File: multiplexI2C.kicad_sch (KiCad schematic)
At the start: 25 parts, among them J17 Conn_01x04_Pin, J18 PinSocket_1x20_P2.54mm_Vertic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, J19 PinSocket_1x20_P2.54mm_Vertic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, J20 Screw_Terminal_01x02, U1 PCA9548ADW

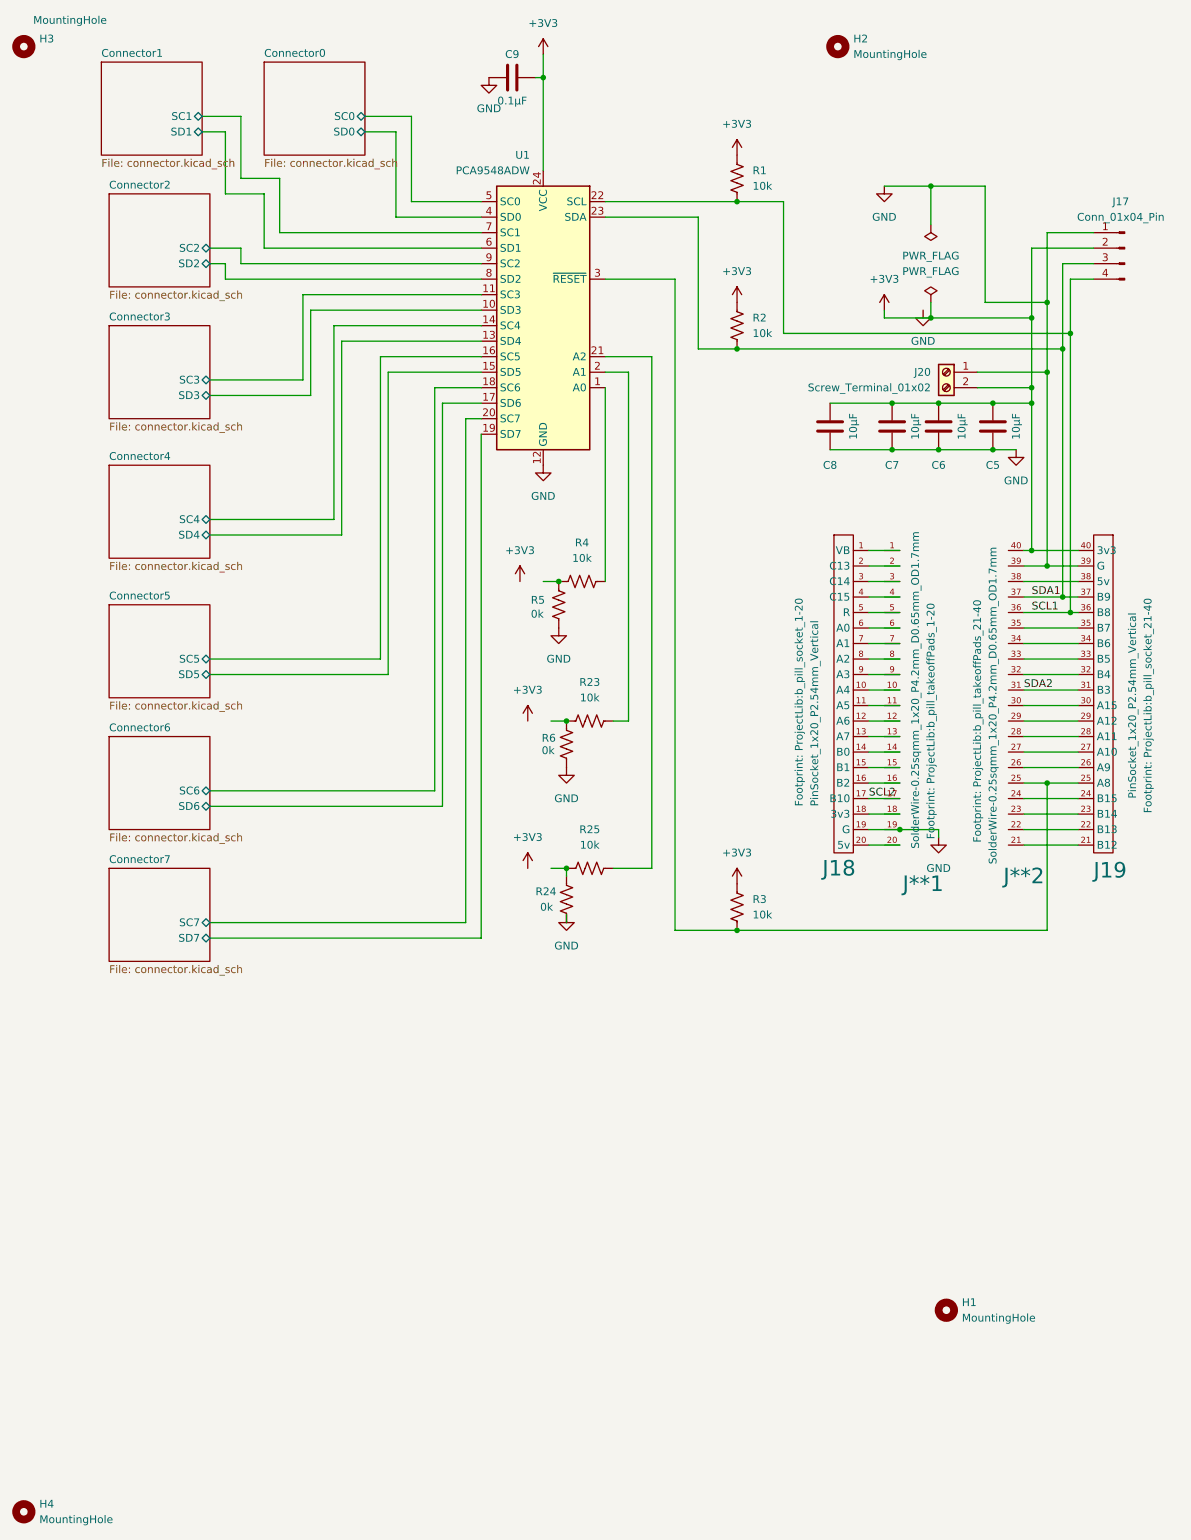
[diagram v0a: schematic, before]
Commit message: ERC and DRC warnings but not erros. Needs some layout adjustments.
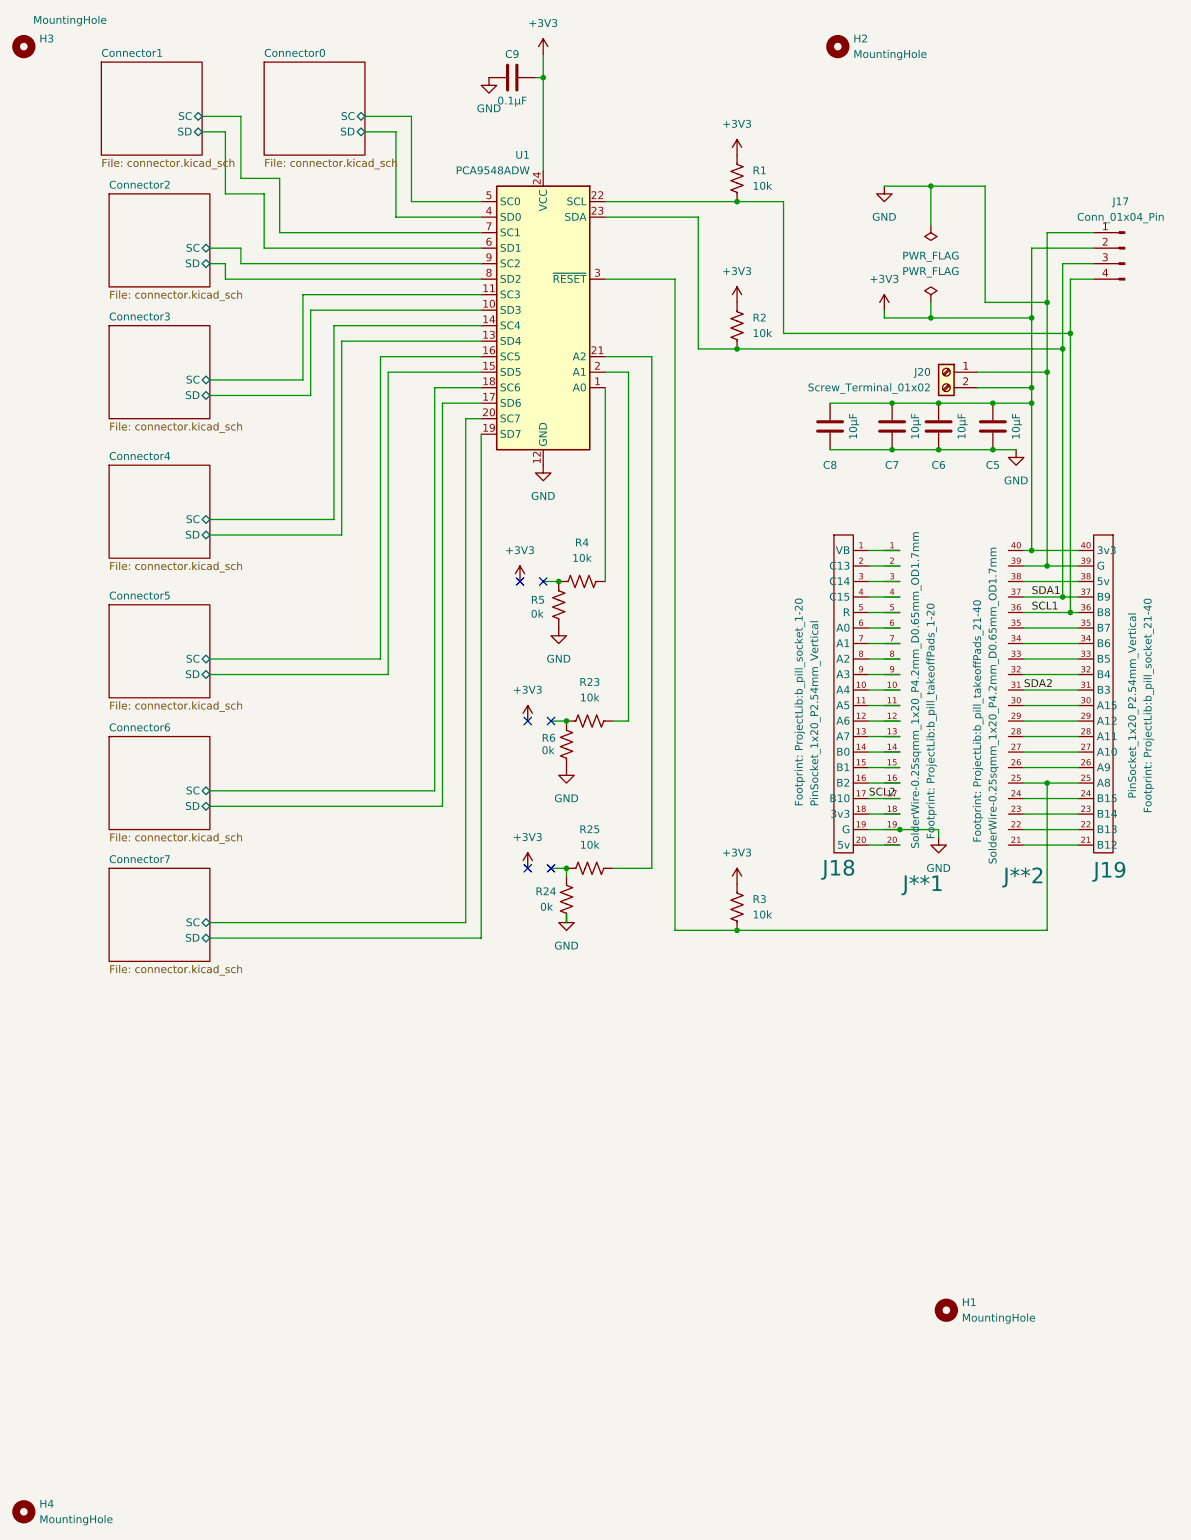
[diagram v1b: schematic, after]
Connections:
- net Connector0/SC0 renamed Connector0/SC
- net Connector0/SD0 renamed Connector0/SD
- net Connector1/SC1 renamed Connector1/SC
- net Connector1/SD1 renamed Connector1/SD
- net Connector2/SC2 renamed Connector2/SC
- net Connector2/SD2 renamed Connector2/SD
- net Connector3/SC3 renamed Connector3/SC
- net Connector3/SD3 renamed Connector3/SD
- net Connector4/SC4 renamed Connector4/SC
- net Connector4/SD4 renamed Connector4/SD
- net Connector5/SC5 renamed Connector5/SC
- net Connector5/SD5 renamed Connector5/SD
- net Connector6/SC6 renamed Connector6/SC
- net Connector6/SD6 renamed Connector6/SD
- net Connector7/SC7 renamed Connector7/SC
- net Connector7/SD7 renamed Connector7/SD
- no-connect marks 0 -> 6
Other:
- sheet Connector0 ports: added SC, SD; removed SC0, SD0
- sheet Connector1 ports: added SC, SD; removed SC1, SD1
- sheet Connector2 ports: added SC, SD; removed SC2, SD2
- sheet Connector3 ports: added SC, SD; removed SC3, SD3
- sheet Connector4 ports: added SC, SD; removed SC4, SD4
- sheet Connector5 ports: added SC, SD; removed SC5, SD5
- sheet Connector6 ports: added SC, SD; removed SC6, SD6
- sheet Connector7 ports: added SC, SD; removed SC7, SD7
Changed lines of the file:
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@@
 		(color 0 0 0 0)
 	)
+	(no_connect
+		(at 105.41 130.81)
+	)
+	(no_connect
+		(at 104.14 107.95)
+	)
+	(no_connect
+		(at 105.41 154.94)
+	)
+	(no_connect
+		(at 101.6 154.94)
+	)
+	(no_connect
+		(at 101.6 130.81)
+	)
+	(no_connect
+		(at 100.33 107.95)
+	)
 	(wire
 		(pts
@@
 	)
 	(symbol
-		(lib_name "GND_1")
-		(lib_id "power:GND")
-		(at 166.37 63.5 0)
-		(unit 1)
-		(exclude_from_sim no)
-		(in_bom yes)
-		(on_board yes)
-		(dnp no)
-		(fields_autoplaced yes)
-		(property "Reference" "#PWR028"
-			(at 166.37 69.85 0)
-			(effects
-				(font
-					(size 1.27 1.27)
-				)
-				(hide yes)
-			)
-		)
-		(property "Value" "GND"
-			(at 166.37 68.58 0)
-			(effects
-				(font
-					(size 1.27 1.27)
-				)
-			)
-		)
-		(property "Footprint" ""
-			(at 166.37 63.5 0)
-			(effects
-				(font
-					(size 1.27 1.27)
-				)
-				(hide yes)
-			)
-		)
-		(property "Datasheet" ""
-			(at 166.37 63.5 0)
-			(effects
-				(font
-					(size 1.27 1.27)
-				)
-				(hide yes)
-			)
-		)
-		(property "Description" "Power symbol creates a global label with name \"GND\" , ground"
-			(at 166.37 63.5 0)
-			(effects
-				(font
-					(size 1.27 1.27)
-				)
-				(hide yes)
-			)
-		)
-		(pin "1"
-		)
-		(instances
-			(project ""
-				(path "/0c2d0c14-8850-4a30-bb78-b2f40cb442ba"
-					(reference "#PWR028")
-					(unit 1)
-				)
-			)
-		)
-	)
-	(symbol
 		(lib_id "power:GND")
 		(at 107.95 162.56 0)
@@
 			)
 		)
-		(pin "SC2" bidirectional
+		(pin "SC" bidirectional
 			(at 49.53 53.34 0)
 			(effects
@@
 			)
 		)
-		(pin "SD2" bidirectional
+		(pin "SD" bidirectional
 			(at 49.53 55.88 0)
 			(effects
@@
 			)
 		)
-		(pin "SC4" bidirectional
+		(pin "SC" bidirectional
 			(at 49.53 97.79 0)
 			(effects
@@
 			)
 		)
-		(pin "SD4" bidirectional
+		(pin "SD" bidirectional
 			(at 49.53 100.33 0)
 			(effects
@@
 			)
 		)
-		(pin "SC7" bidirectional
+		(pin "SC" bidirectional
 			(at 49.53 163.83 0)
 			(effects
@@
 			)
 		)
-		(pin "SD7" bidirectional
+		(pin "SD" bidirectional
 			(at 49.53 166.37 0)
 			(effects
@@
 			)
 		)
-		(pin "SC3" bidirectional
+		(pin "SC" bidirectional
 			(at 49.53 74.93 0)
 			(effects
@@
 			)
 		)
-		(pin "SD3" bidirectional
+		(pin "SD" bidirectional
 			(at 49.53 77.47 0)
 			(effects
@@
 			)
 		)
-		(pin "SC1" bidirectional
+		(pin "SC" bidirectional
 			(at 48.26 31.75 0)
 			(effects
@@
 			)
 		)
-		(pin "SD1" bidirectional
+		(pin "SD" bidirectional
 			(at 48.26 34.29 0)
 			(effects
@@
 			)
 		)
-		(pin "SC6" bidirectional
+		(pin "SC" bidirectional
 			(at 49.53 142.24 0)
 			(effects
@@
 			)
 		)
-		(pin "SD6" bidirectional
+		(pin "SD" bidirectional
 			(at 49.53 144.78 0)
 			(effects
@@
 		(at 58.42 22.86)
 		(size 16.51 15.24)
-		(fields_autoplaced yes)
 		(stroke
 			(width 0.1524)
@@
 			)
 		)
-		(pin "SC0" bidirectional
+		(pin "SC" bidirectional
 			(at 74.93 31.75 0)
 			(effects
@@
 			)
 		)
-		(pin "SD0" bidirectional
+		(pin "SD" bidirectional
 			(at 74.93 34.29 0)
 			(effects
@@
 			)
 		)
-		(pin "SC5" bidirectional
+		(pin "SC" bidirectional
 			(at 49.53 120.65 0)
 			(effects
@@
 			)
 		)
-		(pin "SD5" bidirectional
+		(pin "SD" bidirectional
 			(at 49.53 123.19 0)
 			(effects

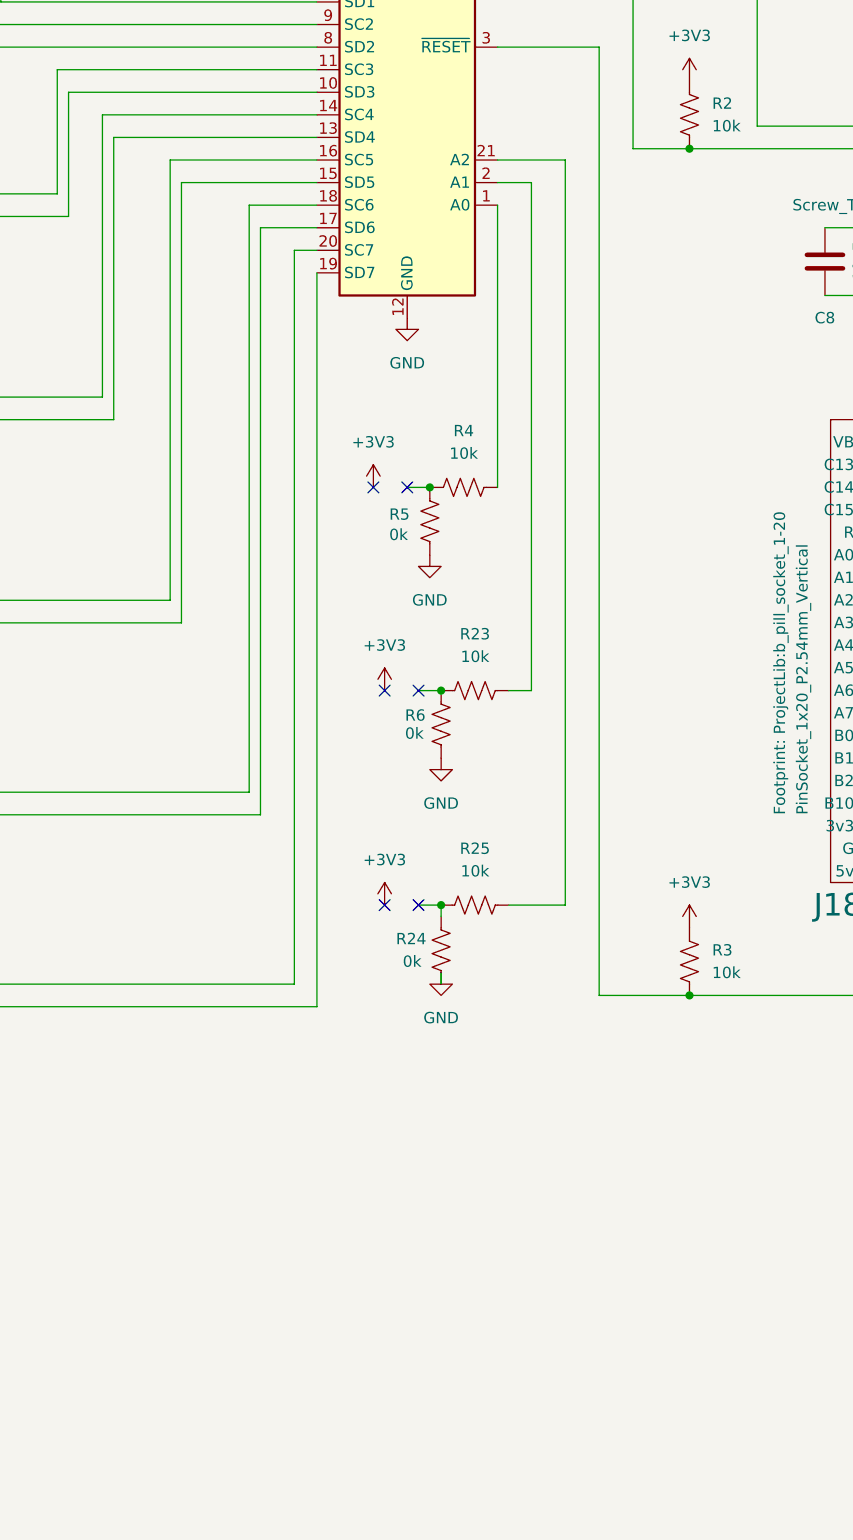
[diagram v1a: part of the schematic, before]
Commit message: no ELC or DRC errors. Still cleaning up warnings. Switched to SW_DIP for PCA9548 address.
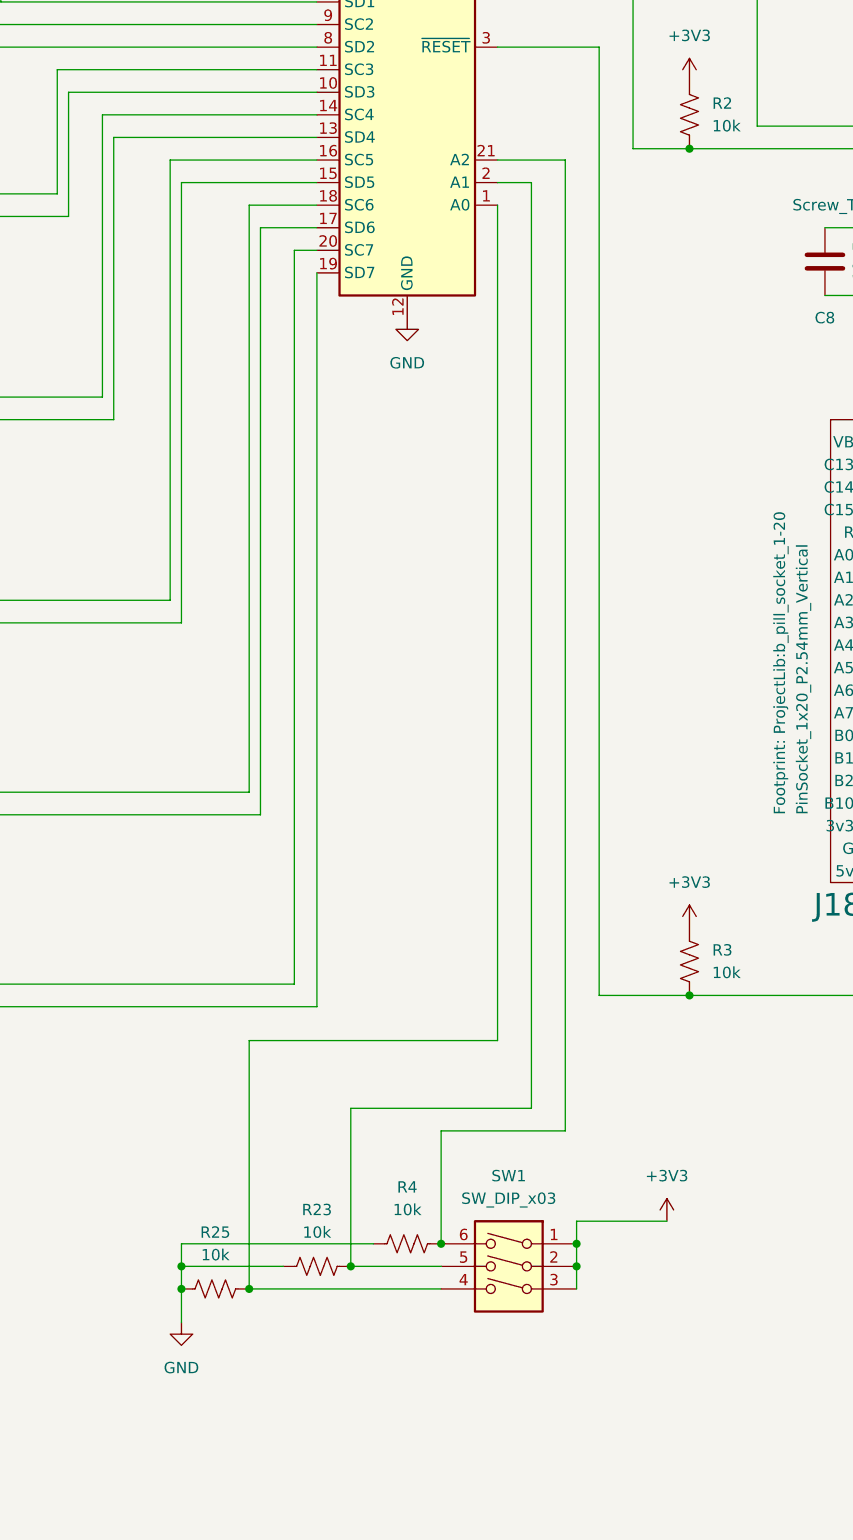
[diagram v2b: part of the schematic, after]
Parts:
- removed R24, R5, R6: 0k, ProjectLib:R_0603_1608Metric, symbol ProjectLib:R_US
- added SW1: SW_DIP_x03, Button_Switch_SMD:SW_DIP_SPSTx03_Slide_KingTek_DSHP03TS_W7.62mm_P1.27mm, symbol Switch:SW_DIP_x03
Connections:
- net +3V3: now also SW1.1, SW1.2, SW1.3
- net GND: now also R23.2, R25.2, R4.2
- net at R23.1, U1.2 (A1): now also SW1.5
- net at R25.1: now also U1.1 (A0), SW1.4; no longer U1.21 (A2)
- net at R4.1: now also U1.21 (A2), SW1.6; no longer U1.1 (A0)
- no-connect marks 6 -> 0
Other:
- moved on the sheet: R23, R25, R4

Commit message: roughly complete, no errors or warnings.
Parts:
- SW1: footprint Button_Switch_SMD:SW_DIP_SPSTx03_Slide_KingTek_DSHP03TS_W7.62mm_P1.27mm -> ProjectLib:SW_DIP_SPSTx03_Slide_KingTek_DSHP03TS_W7.62mm_P1.27mm; symbol Switch:SW_DIP_x03 -> ProjectLib:SW_DIP_x03
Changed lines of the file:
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@@
 		(dnp no)
 		(property "Reference" "C9"
-			(at 99.06 21.59 90)
-			(effects
-				(font
-					(size 1.27 1.27)
-				)
+			(at 99.06 21.59 0)
+			(effects
+				(font
+					(size 1.27 1.27)
+				)
+				(justify left)
 			)
 		)
@@
 					(size 2.54 2.54)
 				)
-				(justify left)
 			)
 		)
@@
 					(size 1.27 1.27)
 				)
-				(justify left)
 			)
 		)
@@
 	)
 	(symbol
-		(lib_id "Switch:SW_DIP_x03")
+		(lib_id "ProjectLib:SW_DIP_x03")
 		(at 115.57 195.58 0)
 		(mirror y)
@@
 			)
 		)
-		(property "Footprint" "Button_Switch_SMD:SW_DIP_SPSTx03_Slide_KingTek_DSHP03TS_W7.62mm_P1.27mm"
+		(property "Footprint" "ProjectLib:SW_DIP_SPSTx03_Slide_KingTek_DSHP03TS_W7.62mm_P1.27mm"
 			(at 115.57 198.12 0)
 			(effects
@@
 					(size 1.27 1.27)
 				)
+				(justify left)
 			)
 		)
@@
 					(size 1.27 1.27)
 				)
-				(justify left)
 			)
 		)
@@
 					(size 1.27 1.27)
 				)
-				(justify left)
 			)
 		)
@@
 					(size 1.27 1.27)
 				)
+				(justify left)
 			)
 		)
@@
 		(fields_autoplaced yes)
 		(property "Reference" "R2"
-			(at 138.43 64.77 0)
-			(effects
-				(font
-					(size 1.27 1.27)
-				)
-				(justify left)
+			(at 138.43 64.77 90)
+			(effects
+				(font
+					(size 1.27 1.27)
+				)
 			)
 		)
@@
 					(size 1.27 1.27)
 				)
-				(justify left)
 			)
 		)
@@
 					(size 1.27 1.27)
 				)
-				(justify left)
 			)
 		)
@@
 		(fields_autoplaced yes)
 		(property "Reference" "R1"
-			(at 138.43 40.64 0)
-			(effects
-				(font
-					(size 1.27 1.27)
-				)
-				(justify left)
+			(at 138.43 40.64 90)
+			(effects
+				(font
+					(size 1.27 1.27)
+				)
 			)
 		)
@@
 					(size 1.27 1.27)
 				)
+				(justify left)
 			)
 		)
@@
 					(size 1.27 1.27)
 				)
+				(justify left)
 			)
 		)
@@
 					(size 1.27 1.27)
 				)
-				(justify left)
 			)
 		)
@@
 		(fields_autoplaced yes)
 		(property "Reference" "R3"
-			(at 138.43 160.02 0)
-			(effects
-				(font
-					(size 1.27 1.27)
-				)
-				(justify left)
-			)
-		)
+			(at 138.43 160.02 90)
+			(effects
+				(font
+					(size 1.27 1.27)
+				)
+			)
+		)

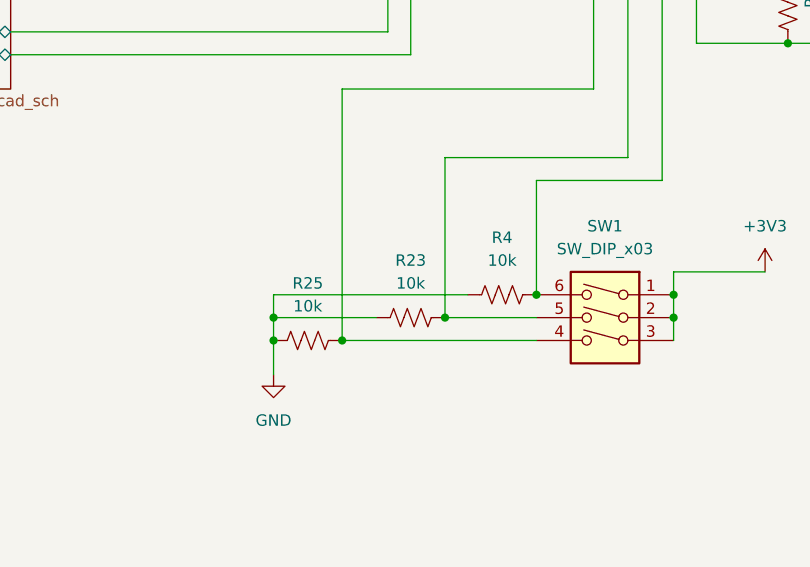
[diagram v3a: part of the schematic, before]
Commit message: put masks on takeoffPads and other ongoing cleanup.
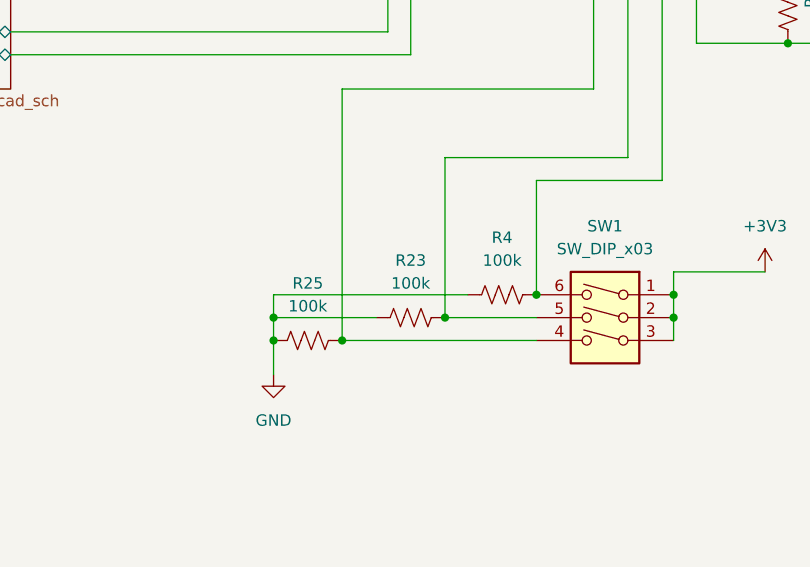
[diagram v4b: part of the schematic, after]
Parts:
- R23, R25, R4: value 10k -> 100k
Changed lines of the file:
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@@
 			)
 		)
-		(property "Value" "10k"
+		(property "Value" "100k"
 			(at 93.98 191.77 90)
 			(effects
@@
 			)
 		)
-		(property "Value" "10k"
+		(property "Value" "100k"
 			(at 82.55 194.31 90)
 			(effects
@@
 			)
 		)
-		(property "Value" "10k"
+		(property "Value" "100k"
 			(at 104.14 189.23 90)
 			(effects
